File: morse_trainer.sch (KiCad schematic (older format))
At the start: 16 parts

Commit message: Schematic done !
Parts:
- added R5: 100, Resistor_SMD:R_0805_2012Metric_Pad1.15x1.40mm_HandSolder, symbol Device:R
- added RV1: 1k, Connector_PinHeader_2.54mm:PinHeader_1x03_P2.54mm_Vertical, symbol Device:R_POT
- BZ1: renamed from BZ?; footprint (none) -> Connector_PinSocket_2.54mm:PinSocket_2x01_P2.54mm_Vertical
- C1, C2: renamed from C?; footprint (none) -> Capacitor_SMD:C_0805_2012Metric_Pad1.15x1.40mm_HandSolder
- C3: renamed from C?; footprint (none) -> Capacitor_THT:CP_Radial_D5.0mm_P2.50mm
- H1, H2: renamed from H?; footprint (none) -> MountingHole:MountingHole_2.2mm_M2
- J1: renamed from J?; footprint (none) -> modules:ISP
- R1, R2, R3, R4, R6: renamed from R?; footprint (none) -> Resistor_SMD:R_0805_2012Metric_Pad1.15x1.40mm_HandSolder
- RV2: renamed from RV?; footprint (none) -> Connector_PinHeader_2.54mm:PinHeader_1x03_P2.54mm_Vertical
- SW1: renamed from SW?; footprint (none) -> Connector_PinHeader_2.54mm:PinHeader_1x02_P2.54mm_Vertical
- U2: renamed from U?; footprint Display:RC1602A -> Connector_PinHeader_2.54mm:PinHeader_1x16_P2.54mm_Vertical
- gave numbers to parts that had none: 1
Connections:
- net MISO is gone; now on net DB7: J1.1 (MISO), U1.18 (PB6)
- net MOSI is gone; now on net DB6: J1.4 (MOSI), U1.17 (PB5)
- net VCC: now also R5.1
- net RS: now reaches U1.12 (PB0)
- net RS: now also U2.4 (RS)
- net R\~W: now reaches U1.13 (PB1)
- net R\~W: now also U2.5 (R/W)
- net E: now reaches U1.14 (PB2)
- net E: now also U2.6 (E)
- net DB4: now reaches U1.15 (PB3)
- net DB4: now also U2.11 (DB4)
- net DB5: now reaches U1.16 (PB4)
- net DB5: now also U2.12 (DB5)
- net DB6: now reaches U2.13 (DB6)
- net DB7: now reaches U2.14 (DB7)
- net at U2.16 (K): now also RV1.2, RV1.3
- new net: R5.2, RV1.1
- no-connect marks 2 -> 6
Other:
- moved on the sheet: R6, RV2

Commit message: Schematics done !
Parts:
- added J2: Conn_01x02, Connector_PinHeader_2.54mm:PinHeader_1x02_P2.54mm_Vertical, symbol Connector_Generic:Conn_01x02
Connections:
- net GND: now also J2.1 (Pin_1)
- net VCC: now also J2.2 (Pin_2)
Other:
- moved on the sheet: C1, C2, C3, J1, R1
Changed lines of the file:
@@
 L Device:R R1
 U 1 1 5D8AE425
-P 2550 3000
-F 0 "R1" H 2620 3046 50  0000 L CNN
-F 1 "1k" H 2620 2955 50  0000 L CNN
-F 2 "Resistor_SMD:R_0805_2012Metric_Pad1.15x1.40mm_HandSolder" V 2480 3000 50  0001 C CNN
-F 3 "~" H 2550 3000 50  0001 C CNN
-	1    2550 3000
+P 2500 4050
+F 0 "R1" H 2570 4096 50  0000 L CNN
+F 1 "1k" H 2570 4005 50  0000 L CNN
+F 2 "Resistor_SMD:R_0805_2012Metric_Pad1.15x1.40mm_HandSolder" V 2430 4050 50  0001 C CNN
+F 3 "~" H 2500 4050 50  0001 C CNN
+	1    2500 4050
 	1    0    0    -1
 $EndComp
@@
 L Device:C C2
 U 1 1 5D8AE4DC
-P 2600 1500
-F 0 "C2" H 2715 1546 50  0000 L CNN
-F 1 "100n" H 2715 1455 50  0000 L CNN
-F 2 "Capacitor_SMD:C_0805_2012Metric_Pad1.15x1.40mm_HandSolder" H 2638 1350 50  0001 C CNN
-F 3 "~" H 2600 1500 50  0001 C CNN
-	1    2600 1500
+P 2200 2100
+F 0 "C2" H 2315 2146 50  0000 L CNN
+F 1 "100n" H 2315 2055 50  0000 L CNN
+F 2 "Capacitor_SMD:C_0805_2012Metric_Pad1.15x1.40mm_HandSolder" H 2238 1950 50  0001 C CNN
+F 3 "~" H 2200 2100 50  0001 C CNN
+	1    2200 2100
 	1    0    0    -1
 $EndComp
@@
 L Device:CP C3
 U 1 1 5D8AE5A3
-P 3100 1500
-F 0 "C3" H 3218 1546 50  0000 L CNN
-F 1 "100u" H 3218 1455 50  0000 L CNN
-F 2 "Capacitor_THT:CP_Radial_D5.0mm_P2.50mm" H 3138 1350 50  0001 C CNN
-F 3 "~" H 3100 1500 50  0001 C CNN
-	1    3100 1500
+P 2700 2100
+F 0 "C3" H 2818 2146 50  0000 L CNN
+F 1 "100u" H 2818 2055 50  0000 L CNN
+F 2 "Capacitor_THT:CP_Radial_D5.0mm_P2.50mm" H 2738 1950 50  0001 C CNN
+F 3 "~" H 2700 2100 50  0001 C CNN
+	1    2700 2100
 	1    0    0    -1
 $EndComp
@@
 L Device:C C1
 U 1 1 5D8AE78E
-P 2550 3950
-F 0 "C1" H 2665 3996 50  0000 L CNN
-F 1 "100n" H 2665 3905 50  0000 L CNN
-F 2 "Capacitor_SMD:C_0805_2012Metric_Pad1.15x1.40mm_HandSolder" H 2588 3800 50  0001 C CNN
-F 3 "~" H 2550 3950 50  0001 C CNN
-	1    2550 3950
+P 2500 5000
+F 0 "C1" H 2615 5046 50  0000 L CNN
+F 1 "100n" H 2615 4955 50  0000 L CNN
+F 2 "Capacitor_SMD:C_0805_2012Metric_Pad1.15x1.40mm_HandSolder" H 2538 4850 50  0001 C CNN
+F 3 "~" H 2500 5000 50  0001 C CNN
+	1    2500 5000
 	1    0    0    -1
 $EndComp
@@
 L Connector:AVR-ISP-6 J1
 U 1 1 5D8AEAA5
-P 1650 3500
-F 0 "J1" H 1370 3596 50  0000 R CNN
-F 1 "AVR-ISP-6" H 1370 3505 50  0000 R CNN
-F 2 "modules:ISP" V 1400 3550 50  0001 C CNN
-F 3 " ~" H 375 2950 50  0001 C CNN
-	1    1650 3500
+P 1600 4550
+F 0 "J1" H 1320 4646 50  0000 R CNN
+F 1 "AVR-ISP-6" H 1320 4555 50  0000 R CNN
+F 2 "modules:ISP" V 1350 4600 50  0001 C CNN
+F 3 " ~" H 325 4000 50  0001 C CNN
+	1    1600 4550
 	1    0    0    -1
 $EndComp
@@
 L power:VCC #PWR01
 U 1 1 5D8AED86
-P 1550 2700
-F 0 "#PWR01" H 1550 2550 50  0001 C CNN
-F 1 "VCC" H 1567 2873 50  0000 C CNN
-F 2 "" H 1550 2700 50  0001 C CNN
-F 3 "" H 1550 2700 50  0001 C CNN
-	1    1550 2700
+P 1500 3750
+F 0 "#PWR01" H 1500 3600 50  0001 C CNN
+F 1 "VCC" H 1517 3923 50  0000 C CNN
+F 2 "" H 1500 3750 50  0001 C CNN
+F 3 "" H 1500 3750 50  0001 C CNN
+	1    1500 3750
 	1    0    0    -1
 $EndComp
@@
 L power:GND #PWR02
 U 1 1 5D8AEEB2
-P 1550 4250
-F 0 "#PWR02" H 1550 4000 50  0001 C CNN
-F 1 "GND" H 1555 4077 50  0000 C CNN
-F 2 "" H 1550 4250 50  0001 C CNN
-F 3 "" H 1550 4250 50  0001 C CNN
-	1    1550 4250
-	1    0    0    -1
-$EndComp
-Wire Wire Line
-	1550 2700 1550 3000
-Wire Wire Line
-	1550 3900 1550 4250
-Wire Wire Line
-	2550 3600 2050 3600
-Wire Wire Line
-	2050 3300 2400 3300
-Wire Wire Line
-	2050 3400 2400 3400
-Wire Wire Line
-	2050 3500 2400 3500
+P 1500 5300
+F 0 "#PWR02" H 1500 5050 50  0001 C CNN
+F 1 "GND" H 1505 5127 50  0000 C CNN
+F 2 "" H 1500 5300 50  0001 C CNN
+F 3 "" H 1500 5300 50  0001 C CNN
+	1    1500 5300
+	1    0    0    -1
+$EndComp
+Wire Wire Line
+	1500 3750 1500 4050
+Wire Wire Line
+	1500 4950 1500 5300
+Wire Wire Line
+	2500 4650 2000 4650
+Wire Wire Line
+	2000 4350 2350 4350
+Wire Wire Line
+	2000 4450 2350 4450
+Wire Wire Line
+	2000 4550 2350 4550
 $Comp
 L power:GND #PWR04
 U 1 1 5D8AF0E3
-P 2550 4250
-F 0 "#PWR04" H 2550 4000 50  0001 C CNN
-F 1 "GND" H 2555 4077 50  0000 C CNN
-F 2 "" H 2550 4250 50  0001 C CNN
-F 3 "" H 2550 4250 50  0001 C CNN
-	1    2550 4250
-	1    0    0    -1
-$EndComp
-Wire Wire Line
-	2550 4250 2550 4100
-Wire Wire Line
-	2550 3800 2550 3600
+P 2500 5300
+F 0 "#PWR04" H 2500 5050 50  0001 C CNN
+F 1 "GND" H 2505 5127 50  0000 C CNN
+F 2 "" H 2500 5300 50  0001 C CNN
+F 3 "" H 2500 5300 50  0001 C CNN
+	1    2500 5300
+	1    0    0    -1
+$EndComp
+Wire Wire Line
+	2500 5300 2500 5150
+Wire Wire Line
+	2500 4850 2500 4650
 $Comp
 L power:VCC #PWR03
 U 1 1 5D8AF23A
-P 2550 2700
-F 0 "#PWR03" H 2550 2550 50  0001 C CNN
-F 1 "VCC" H 2567 2873 50  0000 C CNN
-F 2 "" H 2550 2700 50  0001 C CNN
-F 3 "" H 2550 2700 50  0001 C CNN
-	1    2550 2700
-	1    0    0    -1
-$EndComp
-Wire Wire Line
-	2550 2700 2550 2850
-Wire Wire Line
-	2550 3150 2550 3600
-Connection ~ 2550 3600
+P 2500 3750
+F 0 "#PWR03" H 2500 3600 50  0001 C CNN
+F 1 "VCC" H 2517 3923 50  0000 C CNN
+F 2 "" H 2500 3750 50  0001 C CNN
+F 3 "" H 2500 3750 50  0001 C CNN
+	1    2500 3750
+	1    0    0    -1
+$EndComp
+Wire Wire Line
+	2500 3750 2500 3900
+Wire Wire Line
+	2500 4200 2500 4650
+Connection ~ 2500 4650
 $Comp
 L power:VCC #PWR05
 U 1 1 5D8AF304
-P 2600 1100
-F 0 "#PWR05" H 2600 950 50  0001 C CNN
-F 1 "VCC" H 2617 1273 50  0000 C CNN
-F 2 "" H 2600 1100 50  0001 C CNN
-F 3 "" H 2600 1100 50  0001 C CNN
-	1    2600 1100
+P 2200 1700
+F 0 "#PWR05" H 2200 1550 50  0001 C CNN
+F 1 "VCC" H 2217 1873 50  0000 C CNN
+F 2 "" H 2200 1700 50  0001 C CNN
+F 3 "" H 2200 1700 50  0001 C CNN
+	1    2200 1700
 	1    0    0    -1
 $EndComp
@@
 L power:GND #PWR06
 U 1 1 5D8AF416
-P 2600 1900
-F 0 "#PWR06" H 2600 1650 50  0001 C CNN
-F 1 "GND" H 2605 1727 50  0000 C CNN
-F 2 "" H 2600 1900 50  0001 C CNN
-F 3 "" H 2600 1900 50  0001 C CNN
-	1    2600 1900
-	1    0    0    -1
-$EndComp
-Wire Wire Line
-	2600 1900 2600 1750
-Wire Wire Line
-	2600 1750 3100 1750
-Wire Wire Line
-	3100 1750 3100 1650
-Connection ~ 2600 1750
-Wire Wire Line
-	2600 1750 2600 1650
-Wire Wire Line
-	3100 1350 3100 1250
-Wire Wire Line
-	3100 1250 2600 1250
-Wire Wire Line
-	2600 1250 2600 1350
-Wire Wire Line
-	2600 1250 2600 1100
-Connection ~ 2600 1250
+P 2200 2500
+F 0 "#PWR06" H 2200 2250 50  0001 C CNN
+F 1 "GND" H 2205 2327 50  0000 C CNN
+F 2 "" H 2200 2500 50  0001 C CNN
+F 3 "" H 2200 2500 50  0001 C CNN
+	1    2200 2500
+	1    0    0    -1
+$EndComp
+Wire Wire Line
+	2200 2500 2200 2350
+Wire Wire Line
+	2200 2350 2700 2350
+Wire Wire Line
+	2700 2350 2700 2250
+Connection ~ 2200 2350
+Wire Wire Line
+	2200 2350 2200 2250
+Wire Wire Line
+	2700 1950 2700 1850
+Wire Wire Line
+	2700 1850 2200 1850
+Wire Wire Line
+	2200 1850 2200 1950
+Wire Wire Line
+	2200 1850 2200 1700
+Connection ~ 2200 1850
 Text Label 5500 3200 2    50   ~ 0
 SCK
@@
 NoConn ~ 4000 2900
 NoConn ~ 4000 2700
-Text Label 2400 3500 2    50   ~ 0
+Text Label 2350 4550 2    50   ~ 0
 SCK
-Text Label 2400 3300 2    50   ~ 0
+Text Label 2350 4350 2    50   ~ 0
 MISO
-Text Label 2400 3400 2    50   ~ 0
+Text Label 2350 4450 2    50   ~ 0
 MOSI
-Text Label 2400 3600 2    50   ~ 0
+Text Label 2350 4650 2    50   ~ 0
 ~RST
 $Comp
@@
 Wire Wire Line
 	10150 1950 10350 1950
+Wire Wire Line
+	1600 2000 1850 2000
+Wire Wire Line
+	1850 2000 1850 1850
+Wire Wire Line
+	1850 1850 2200 1850
+Wire Wire Line
+	2200 2350 1850 2350
+Wire Wire Line
+	1600 2100 1850 2100
+$Comp
+L Connector_Generic:Conn_01x02 J2
+U 1 1 5D8D8C0E
+P 1400 2100
+F 0 "J2" H 1320 1775 50  0000 C CNN
+F 1 "Conn_01x02" H 1320 1866 50  0000 C CNN
+F 2 "Connector_PinHeader_2.54mm:PinHeader_1x02_P2.54mm_Vertical" H 1400 2100 50  0001 C CNN
+F 3 "~" H 1400 2100 50  0001 C CNN
+	1    1400 2100
+	-1   0    0    1
+$EndComp
+Wire Wire Line
+	1850 2100 1850 2350
 $EndSCHEMATC

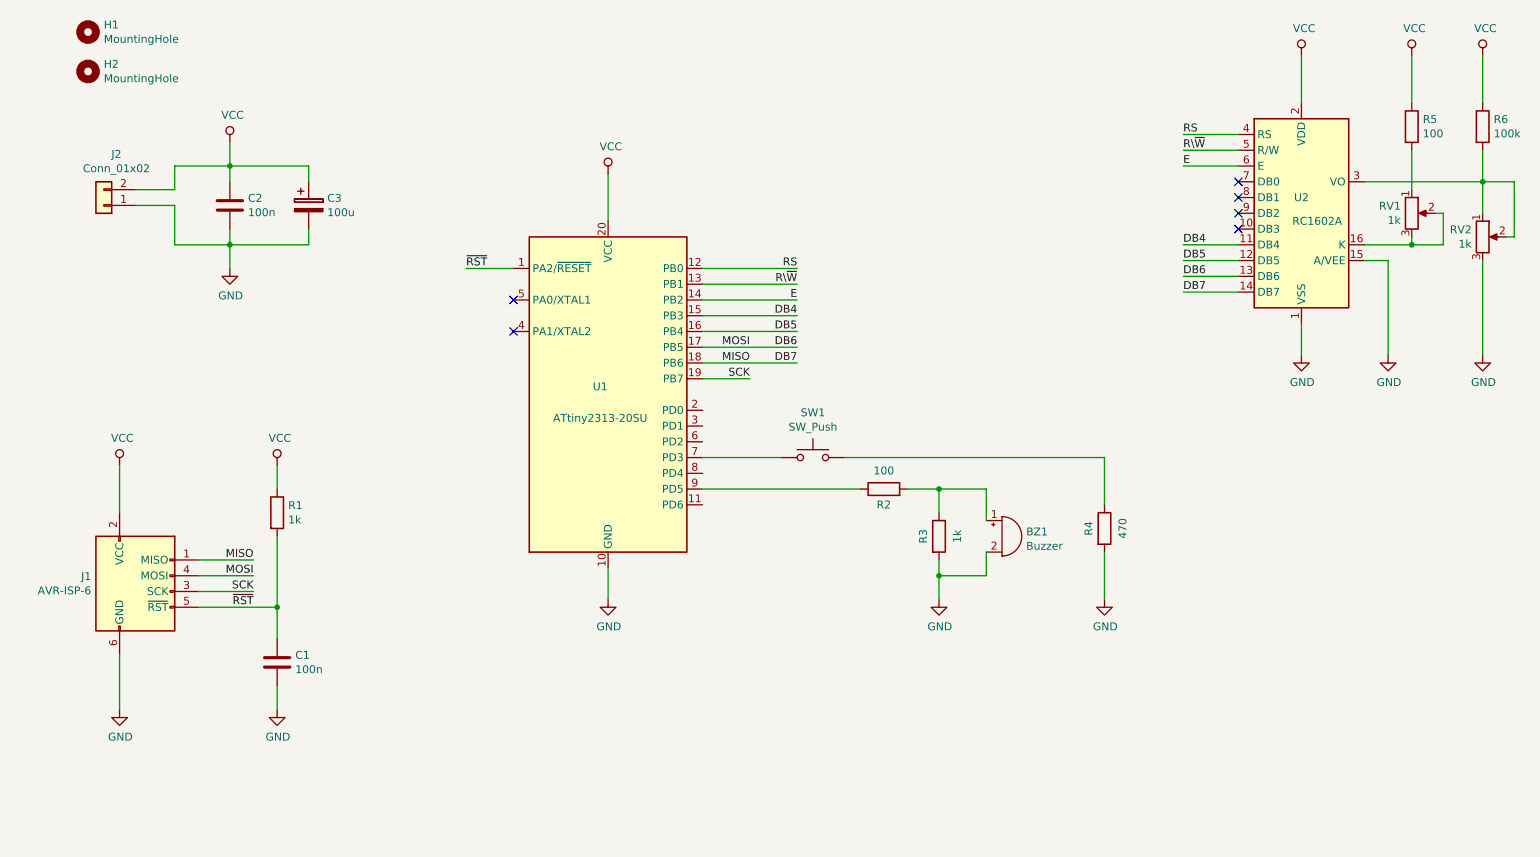
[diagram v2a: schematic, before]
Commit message: add 2 10 pin connector to the schematic \n first version of the boad is done
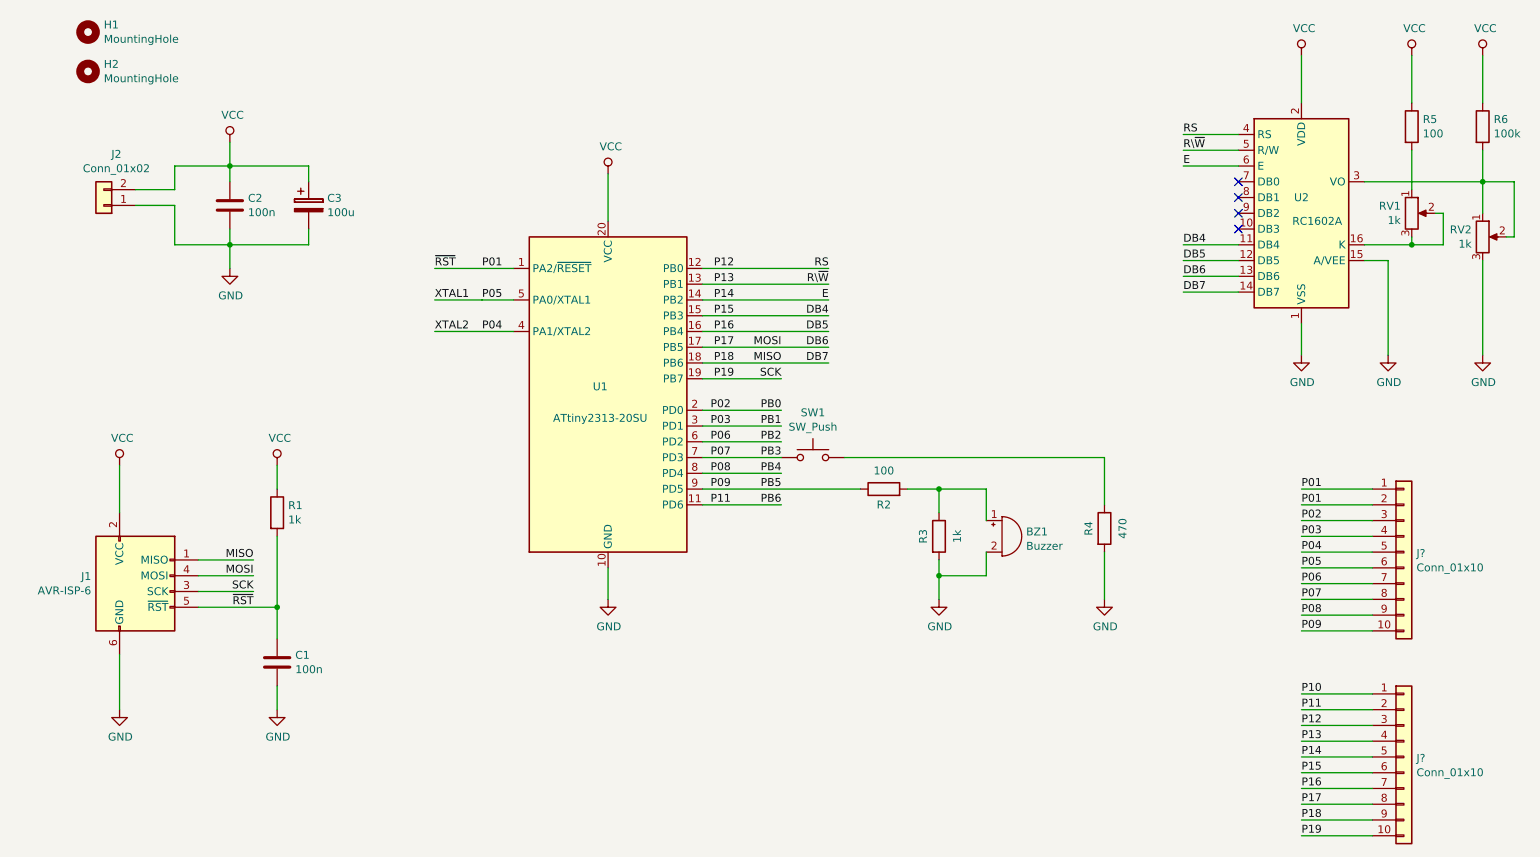
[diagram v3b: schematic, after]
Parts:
- added J? (x2): Conn_01x10, symbol Connector_Generic:Conn_01x10
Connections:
- net DB4: now also J?.6 (Pin_6)
- net DB5: now also J?.7 (Pin_7)
- net DB6: now also J?.8 (Pin_8)
- net DB7: now also J?.9 (Pin_9)
- net E: now also J?.5 (Pin_5)
- net P11: now reaches U1.11 (PD6)
- net P11: now also J?.2 (Pin_2)
- net P02: now reaches U1.2 (PD0)
- net P02: now also J?.3 (Pin_3)
- net P03: now reaches U1.3 (PD1)
- net P03: now also J?.4 (Pin_4)
- net P04: now reaches U1.4 (PA1/XTAL2)
- net P04: now also J?.5 (Pin_5)
- net P05: now reaches U1.5 (PA0/XTAL1)
- net P05: now also J?.6 (Pin_6)
- net P06: now reaches U1.6 (PD2)
- net P06: now also J?.7 (Pin_7)
- net P07: now reaches SW1.1, U1.7 (PD3)
- net P07: now also J?.8 (Pin_8)
- net P08: now reaches U1.8 (PD4)
- net P08: now also J?.9 (Pin_9)
- net P09: now reaches R2.1, U1.9 (PD5)
- net P09: now also J?.10 (Pin_10)
- net RS renamed P12
- net P12: now also J?.3 (Pin_3)
- net R\~W renamed P13
- net P13: now also J?.4 (Pin_4)
- net SCK renamed P19
- net P19: now also J?.10 (Pin_10)
- net ~RST renamed P01
- net P01: now also J?.1 (Pin_1), J?.2 (Pin_2)
- new net P10: J?.1 (Pin_1)
- no-connect marks 6 -> 4
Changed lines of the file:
@@
 	2200 1850 2200 1700
 Connection ~ 2200 1850
-Text Label 5500 3200 2    50   ~ 0
+Text Label 5700 3200 2    50   ~ 0
 SCK
-Text Label 5500 3100 2    50   ~ 0
+Text Label 5700 3100 2    50   ~ 0
 MISO
-Text Label 5500 3000 2    50   ~ 0
+Text Label 5700 3000 2    50   ~ 0
 MOSI
-Text Label 3700 2500 0    50   ~ 0
+Text Label 3500 2500 0    50   ~ 0
 ~RST
-Wire Wire Line
-	4000 2500 3700 2500
-Wire Wire Line
-	5500 3200 5200 3200
 $Comp
 L Switch:SW_Push SW1
@@
 Wire Wire Line
 	7750 4000 7750 3700
-NoConn ~ 4000 2900
-NoConn ~ 4000 2700
 Text Label 2350 4550 2    50   ~ 0
 SCK
@@
 NoConn ~ 8600 2150
 NoConn ~ 8600 2250
-Wire Wire Line
-	5200 2500 5800 2500
-Wire Wire Line
-	5200 2600 5800 2600
-Wire Wire Line
-	5200 2700 5800 2700
-Wire Wire Line
-	5200 2800 5800 2800
-Wire Wire Line
-	5200 2900 5800 2900
-Text Label 5800 2500 2    50   ~ 0
+Text Label 6000 2500 2    50   ~ 0
 RS
-Text Label 5800 2600 2    50   ~ 0
+Text Label 6000 2600 2    50   ~ 0
 R\~W
-Text Label 5800 2700 2    50   ~ 0
+Text Label 6000 2700 2    50   ~ 0
 E
-Text Label 5800 2800 2    50   ~ 0
+Text Label 6000 2800 2    50   ~ 0
 DB4
-Text Label 5800 2900 2    50   ~ 0
+Text Label 6000 2900 2    50   ~ 0
 DB5
-Text Label 5800 3000 2    50   ~ 0
+Text Label 6000 3000 2    50   ~ 0
 DB6
-Text Label 5800 3100 2    50   ~ 0
+Text Label 6000 3100 2    50   ~ 0
 DB7
 $Comp
@@
 Wire Wire Line
 	9700 1150 9700 1450
-Wire Wire Line
-	5200 3000 5800 3000
-Wire Wire Line
-	5200 3100 5800 3100
 Wire Wire Line
 	9700 1750 9700 2000
@@
 Wire Wire Line
 	1850 2100 1850 2350
+Wire Wire Line
+	5200 3400 5700 3400
+Wire Wire Line
+	5200 3500 5700 3500
+Wire Wire Line
+	5200 3600 5700 3600
+Wire Wire Line
+	5200 3800 5700 3800
+Wire Wire Line
+	5200 4000 5700 4000
+Text Label 5700 3400 2    50   ~ 0
+PB0
+Text Label 5700 3500 2    50   ~ 0
+PB1
+Text Label 5700 3600 2    50   ~ 0
+PB2
+Text Label 5700 3700 2    50   ~ 0
+PB3
+Text Label 5700 3800 2    50   ~ 0
+PB4
+Text Label 5700 3900 2    50   ~ 0
+PB5
+Text Label 5700 4000 2    50   ~ 0
+PB6
+Wire Wire Line
+	3500 2700 3800 2700
+Wire Wire Line
+	3800 2900 3500 2900
+Text Label 3500 2700 0    50   ~ 0
+XTAL1
+Text Label 3500 2900 0    50   ~ 0
+XTAL2
+$Comp
+L Connector_Generic:Conn_01x10 J?
+U 1 1 5ED7C278
+P 9650 4300
+F 0 "J?" H 9730 4292 50  0000 L CNN
+F 1 "Conn_01x10" H 9730 4201 50  0000 L CNN
+F 2 "" H 9650 4300 50  0001 C CNN
+F 3 "~" H 9650 4300 50  0001 C CNN
+	1    9650 4300
+	1    0    0    -1
+$EndComp
+$Comp
+L Connector_Generic:Conn_01x10 J?
+U 1 1 5ED7C3AC
+P 9650 5600
+F 0 "J?" H 9730 5592 50  0000 L CNN
+F 1 "Conn_01x10" H 9730 5501 50  0000 L CNN
+F 2 "" H 9650 5600 50  0001 C CNN
+F 3 "~" H 9650 5600 50  0001 C CNN
+	1    9650 5600
+	1    0    0    -1
+$EndComp
+Wire Wire Line
+	9450 3900 9000 3900
+Wire Wire Line
+	9450 4000 9000 4000
+Wire Wire Line
+	9450 4100 9000 4100
+Wire Wire Line
+	9450 4200 9000 4200
+Wire Wire Line
+	9450 4300 9000 4300
+Wire Wire Line
+	9450 4400 9000 4400
+Wire Wire Line
+	9450 4500 9000 4500
+Wire Wire Line
+	9450 4600 9000 4600
+Wire Wire Line
+	9450 4700 9000 4700
+Wire Wire Line
+	9450 4800 9000 4800
+Wire Wire Line
+	9450 5200 9000 5200
+Wire Wire Line
+	9450 5300 9000 5300
+Wire Wire Line
+	9450 5400 9000 5400
+Wire Wire Line
+	9450 5500 9000 5500
+Wire Wire Line
+	9450 5600 9000 5600
+Wire Wire Line
+	9450 5700 9000 5700
+Wire Wire Line
+	9450 5800 9000 5800
+Wire Wire Line
+	9450 5900 9000 5900
+Wire Wire Line
+	9450 6000 9000 6000
+Wire Wire Line
+	9450 6100 9000 6100
+Text Label 5400 2500 2    50   ~ 0
+P12
+Text Label 5400 2600 2    50   ~ 0
+P13
+Text Label 5400 2700 2    50   ~ 0
+P14
+Text Label 5400 2800 2    50   ~ 0
+P15
+Text Label 5400 2900 2    50   ~ 0
+P16
+Text Label 5400 3000 2    50   ~ 0
+P17
+Text Label 5400 3100 2    50   ~ 0
+P18
+Text Label 5400 3200 2    50   ~ 0
+P19
+Wire Wire Line
+	5200 2500 6000 2500
+Text Label 5250 3400 0    50   ~ 0
+P02
+Text Label 5250 3500 0    50   ~ 0
+P03
+Text Label 5250 3600 0    50   ~ 0
+P06
+Text Label 5250 3700 0    50   ~ 0
+P07
+Text Label 5250 3800 0    50   ~ 0
+P08
+Text Label 5250 3900 0    50   ~ 0
+P09
+Text Label 5250 4000 0    50   ~ 0
+P11
+Wire Wire Line
+	5200 2600 6000 2600
+Wire Wire Line
+	5200 2700 6000 2700
+Wire Wire Line
+	5200 2800 6000 2800
+Wire Wire Line
+	5200 2900 6000 2900
+Wire Wire Line
+	5200 3000 6000 3000
+Wire Wire Line
+	5200 3100 6000 3100
+Wire Wire Line
+	5200 3200 5700 3200
+Wire Wire Line
+	3500 2500 4000 2500
+Wire Wire Line
+	3800 2700 4000 2700
+Wire Wire Line
+	3800 2900 4000 2900
+Text Label 3800 2500 0    50   ~ 0
+P01
+Text Label 3800 2900 0    50   ~ 0
+P04
+Text Label 3800 2700 0    50   ~ 0
+P05
+Text Label 9000 3900 0    50   ~ 0
+P01
+Text Label 9000 4000 0    50   ~ 0
+P01
+Text Label 9000 4100 0    50   ~ 0
+P02
+Text Label 9000 4200 0    50   ~ 0
+P03
+Text Label 9000 4300 0    50   ~ 0
+P04
+Text Label 9000 4400 0    50   ~ 0
+P05
+Text Label 9000 4500 0    50   ~ 0
+P06
+Text Label 9000 4600 0    50   ~ 0
+P07
+Text Label 9000 4700 0    50   ~ 0
+P08
+Text Label 9000 4800 0    50   ~ 0
+P09
+Text Label 9000 5200 0    50   ~ 0
+P10
+Text Label 9000 5300 0    50   ~ 0
+P11
+Text Label 9000 5400 0    50   ~ 0
+P12
+Text Label 9000 5500 0    50   ~ 0
+P13
+Text Label 9000 5600 0    50   ~ 0
+P14
+Text Label 9000 5700 0    50   ~ 0
+P15
+Text Label 9000 5800 0    50   ~ 0
+P16
+Text Label 9000 5900 0    50   ~ 0
+P17
+Text Label 9000 6000 0    50   ~ 0
+P18
+Text Label 9000 6100 0    50   ~ 0
+P19
 $EndSCHEMATC
